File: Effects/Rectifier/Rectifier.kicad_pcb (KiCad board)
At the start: 4 copper layers, 32 x 60 mm, 36 parts, among them J1 Conn_02x04_Odd_Even, J2 Conn_02x04_Odd_Even, SW1 SW_SPDT, U1 OPA1656, U2 BUF634AxD, U3 OPA1656

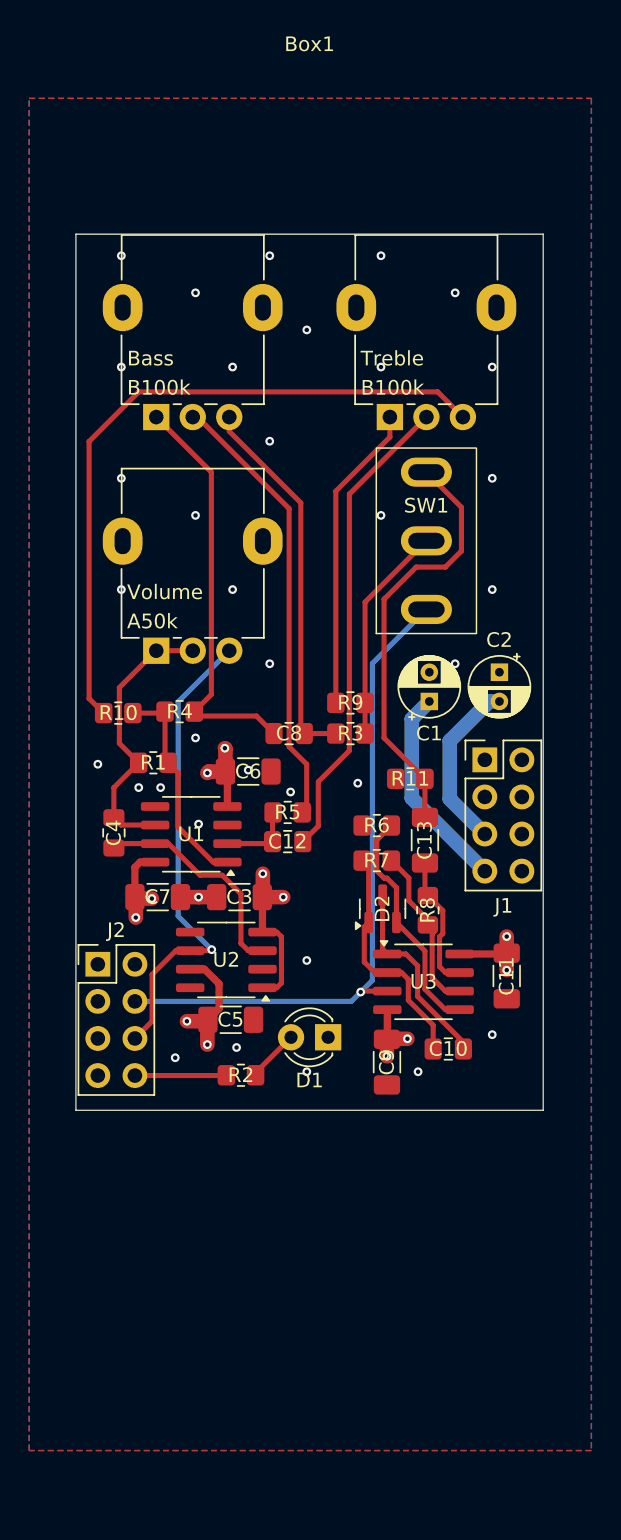
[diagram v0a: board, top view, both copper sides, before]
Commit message: Octaver: replace the effect switch with a blending pot
Instead of a hard switch between octaver circuit bypass, use a pot and
another op-amp to blend the original and the rectified signal before the
tone control.

To make it all simpler, this removes the DC bias after blending, so that
the blending inputs are both driven similarly directly from the previous
op-amp.

It shouldn't matter - the blending stage will happily blend in the DC
offset and while it conceptually makes more sense after the
rectification stage rather than the blending stage, the end result is
the same.

Let's hope the end result is "it works". That would be good.

Signed-off-by: Linus Torvalds <torvalds@linux-foundation.org>
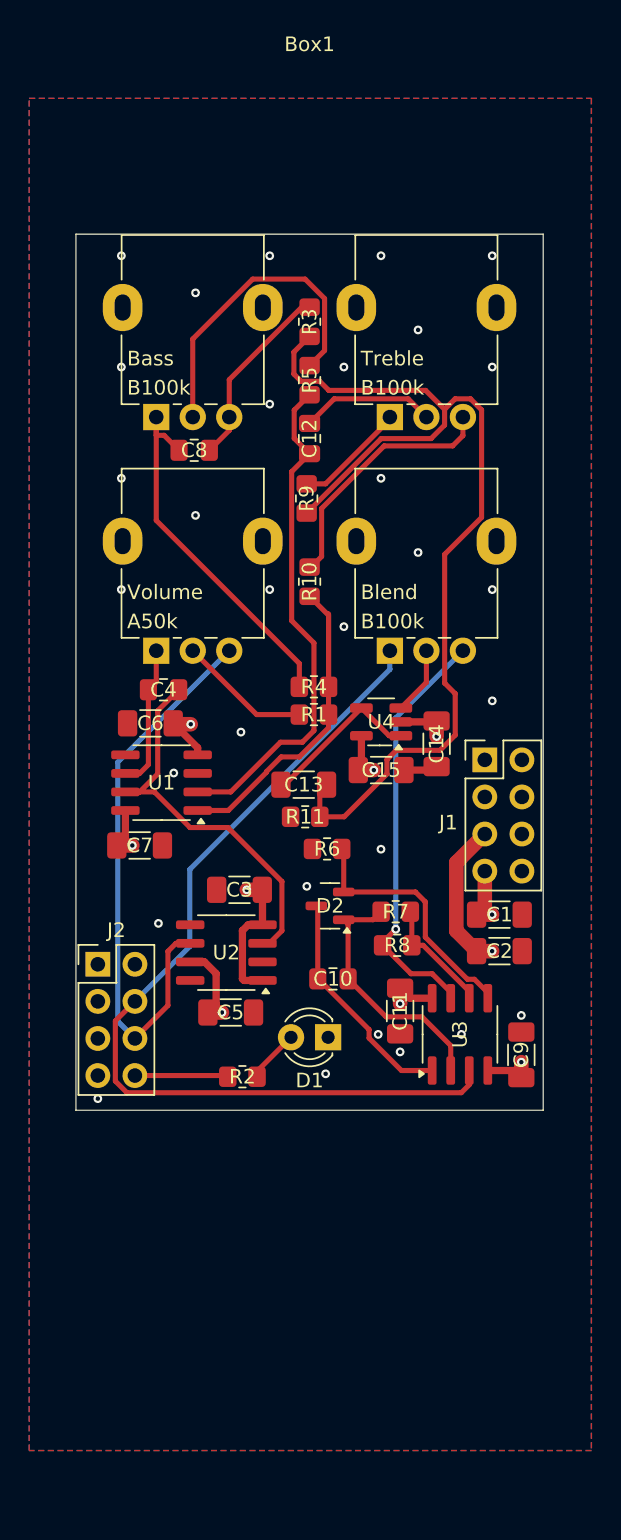
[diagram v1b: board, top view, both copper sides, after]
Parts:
- removed SW1: SW_SPDT, Mylib:Tayda Toggle SPDT
- added C14: 0.1uF, Capacitor_SMD:C_1206_3216Metric_Pad1.33x1.80mm_HandSolder, F.Cu at (108.7, 97.9)
- added C15: 0.1uF, Capacitor_SMD:C_1206_3216Metric_Pad1.33x1.80mm_HandSolder, F.Cu at (104.9, 99.7)
- added RV4: Blend B100k, Potentiometer_THT:Potentiometer_Alpha_RD901F-40-00D_Single_Vertical, F.Cu at (105.5, 91.5)
- added U4: OPA1655, Package_TO_SOT_SMD:SOT-23-5_HandSoldering, F.Cu at (104.9, 96.4)
- C1, C2: footprint Capacitor_THT:CP_Radial_D4.0mm_P2.00mm -> Capacitor_SMD:C_1206_3216Metric_Pad1.33x1.80mm_HandSolder
- R11: value 470k -> 1M0
- moved R5 29.6 mm to (100.0, 73.0), turned to -90 degrees
- moved R3 28.3 mm to (100.0, 69.0), turned to -90 degrees
- moved C12 27.6 mm to (100.0, 77.0), turned to 90 degrees
- moved C8 20.5 mm to (92.1, 77.8)
- moved C2 19.1 mm to (113.0, 112.1), turned to 0 degrees
- moved R10 15.9 mm to (100.0, 86.8), turned to 90 degrees
- moved C1 15.4 mm to (113.0, 109.6), turned to 0 degrees
- moved R9 14.3 mm to (99.8, 81.1), turned to -90 degrees
- moved R1 11.5 mm to (100.3, 95.9)
- moved C4 10.4 mm to (90.0, 94.2), turned to 180 degrees
- moved R4 9.36 mm to (100.3, 94.0), turned to 180 degrees
- moved C10 9.24 mm to (101.6, 114.0), turned to 180 degrees
- moved C9 9.21 mm to (114.5, 119.2), turned to 90 degrees
- moved C13 9.13 mm to (99.6, 100.7), turned to 0 degrees
- moved C11 7.68 mm to (106.2, 116.2)
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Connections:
- C13 pad 1: OUT^{RECT} -> Net-(U4--)
- C13 pad 2: Net-(SW1-C) -> IN^{TONE}
- C2 pad 1: GND -> -V
- C2 pad 2: -V -> GND
- R11 pad 2: Net-(SW1-C) -> IN^{TONE}
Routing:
- net IN^{TONE}: track 14.9 -> 68.0 mm
- net Net-(R10-Pad2): track 46.7 -> 17.3 mm
- net Net-(U1A--): track 4.91 -> 34.2 mm
- net Net-(SW1-C): track 29.2 -> 0.00 mm
- net +V: track 108.3 -> 81.6 mm, vias 6 -> 5
- net Net-(C12-Pad2): track 32.6 -> 9.22 mm
- net OUT^{RECT}: track 8.96 -> 28.3 mm, vias 0 -> 1
- net IN^{EFF}: track 45.6 -> 63.0 mm, vias 1 -> 0
- net Net-(R9-Pad1): track 21.1 -> 7.69 mm
- net Net-(C8-Pad1): track 26.0 -> 13.0 mm
- net Net-(U1B-OUT): track 14.9 -> 26.9 mm
- net Net-(U4--): track 0.00 -> 10.9 mm
- net OUT^{BAX}: track 14.5 -> 24.8 mm
- net Net-(R5-Pad1): track 29.9 -> 21.6 mm
- net OUT^{EFF}: track 32.5 -> 38.9 mm, vias 1 -> 0
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
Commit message: Convert the USB LDO base board and the Octaver to 2-layer boards
I said I wouldn't do this, because 4-layer boards just makes it easier
being lazy, and doesn't involve messing up the gerbers by switching
stack-up in the middle of the project.

But I wanted to see how painful it would be, particularly with the
fairly packed Octaver board (well, packed for _me_, not like it's
actually all that full).

The inner layers were pretty empty anyway, since I tend to try to avoid
via routing and mainly used them for some power routing, and it really
wasn't that much work.

I've switched to the new smaller Murata caps on these boards at the same
time.

Signed-off-by: Linus Torvalds <torvalds@linux-foundation.org>
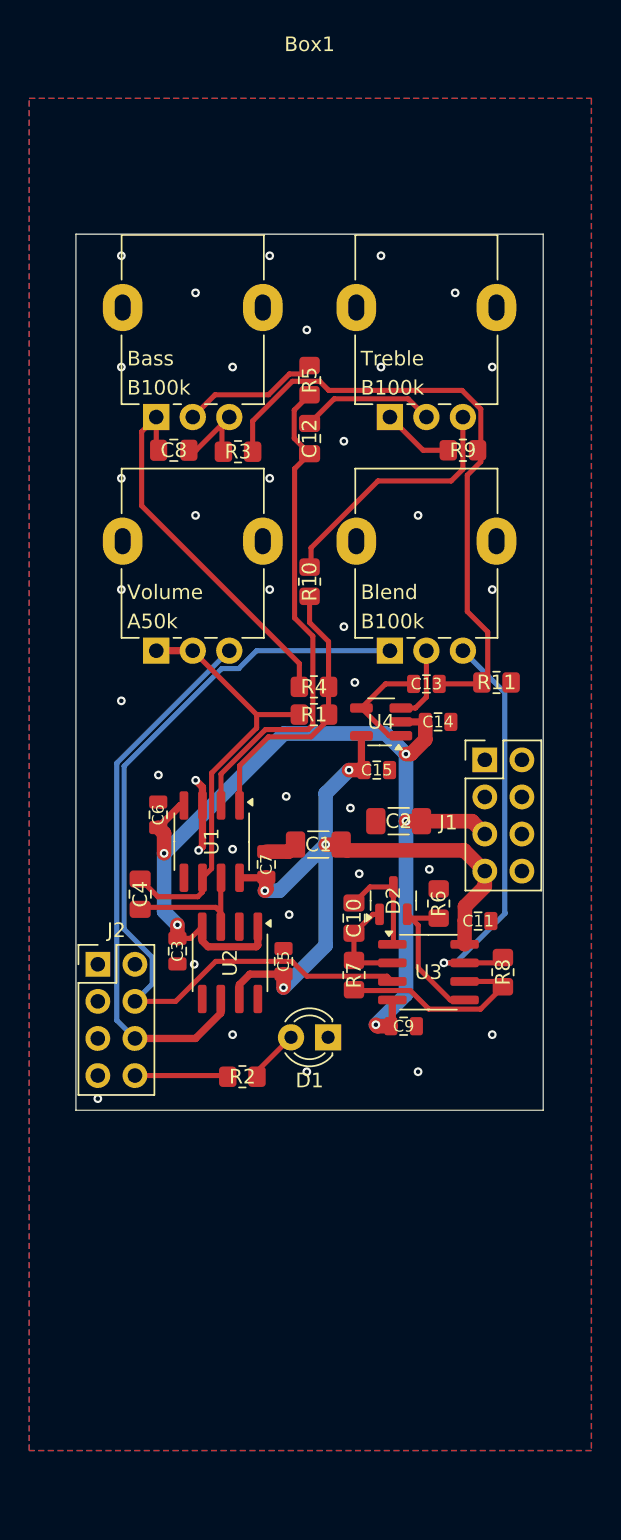
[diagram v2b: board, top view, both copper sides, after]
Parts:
- C11, C13, C14, C15, C3, C5, C6, C7, C9: footprint Capacitor_SMD:C_1206_3216Metric_Pad1.33x1.80mm_HandSolder -> Mylib:C_0704_1810Metric
- moved R11 16.0 mm to (112.8, 93.7), turned to 180 degrees
- moved C4 14.1 mm to (88.4, 108.2), turned to 90 degrees
- moved C1 13.3 mm to (100.6, 104.8), turned to 180 degrees
- moved C2 11.3 mm to (106.1, 103.2), turned to 180 degrees
- moved R9 11.2 mm to (110.5, 77.8), turned to 0 degrees
- moved C13 10.9 mm to (108.0, 93.8)
- moved R3 10.2 mm to (95.1, 77.9), turned to 0 degrees
- moved C7 8.77 mm to (97.0, 106.2), turned to 90 degrees
- moved R6 8.51 mm to (108.8, 108.8), turned to -90 degrees
- moved C9 8.29 mm to (106.4, 117.2), turned to 0 degrees
- moved C11 8.15 mm to (111.5, 110.0), turned to 0 degrees
- moved R8 7.47 mm to (113.2, 113.5), turned to 90 degrees
- moved C6 6.29 mm to (89.6, 102.8), turned to 90 degrees
- moved C3 5.97 mm to (91.0, 112.1), turned to -90 degrees
- moved U1 5.30 mm to (93.3, 104.6), turned to -90 degrees
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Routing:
- net +V: track 81.6 -> 50.6 mm, vias 5 -> 4
- net IN^{TONE}: track 68.0 -> 41.8 mm
- net Net-(U1B-OUT): track 26.9 -> 9.83 mm
- net -V: track 87.4 -> 71.8 mm
- net Net-(R5-Pad1): track 21.6 -> 9.46 mm
- net Net-(D2A-A): track 17.6 -> 6.61 mm
- net Net-(U1B--): track 21.5 -> 30.2 mm
- net Net-(D2A-K): track 15.7 -> 7.01 mm
- net Net-(C8-Pad1): track 13.0 -> 5.48 mm
- net Net-(D2B-common): track 17.0 -> 10.3 mm
- net Net-(U3B--): track 7.44 -> 13.6 mm
- net OUT^{BAX}: track 24.8 -> 18.8 mm
- net GND: track 2.00 -> 7.64 mm, vias 30 -> 36
- net IN^{EFF}: track 63.0 -> 58.2 mm
- net Net-(U4--): track 10.9 -> 7.75 mm
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- removed copper zone on In1.Cu, net GND
- removed copper zone on In2.Cu, net GND
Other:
- copper layers 4 -> 2
